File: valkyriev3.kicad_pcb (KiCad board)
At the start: 4 copper layers, 70 x 100 mm, 125 parts, among them J1 USB_C_Receptacle_USB2.0_16P, J10 Conn_01x03, J11 Conn_01x03, J2 DE9_Pins_MountingHoles, J3 SMA_180C, J4 SMA_180C, J5 Conn_01x02_Socket, J6 Conn_01x02_Socket, J7 Conn_01x02_Socket, J8 Conn_01x03, J9 Conn_01x05, Q1 BC817, Q2 BC817, Q3 BC817, Q4 BC817, Q5 BC817, Q6 DMG3420U, Q7 DMP2305U, Q8 DMG3420U, SW1 SW_SPST, SW2 SW_SPST, U1 W25Q128JVS, U10 LPS22HB, U2 ESP32-S3-MINI-1U, U3 MAX3232, U4 AMS1117-3.3, U5 TPS562202, U9 MS5607-02BA

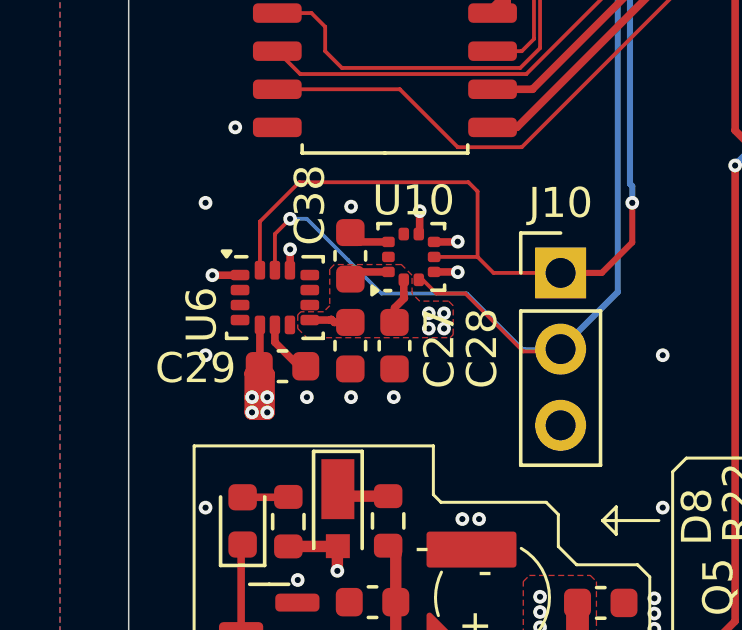
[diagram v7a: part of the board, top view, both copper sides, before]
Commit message: connected IMU pins 7 and 9 to GND instead of NC
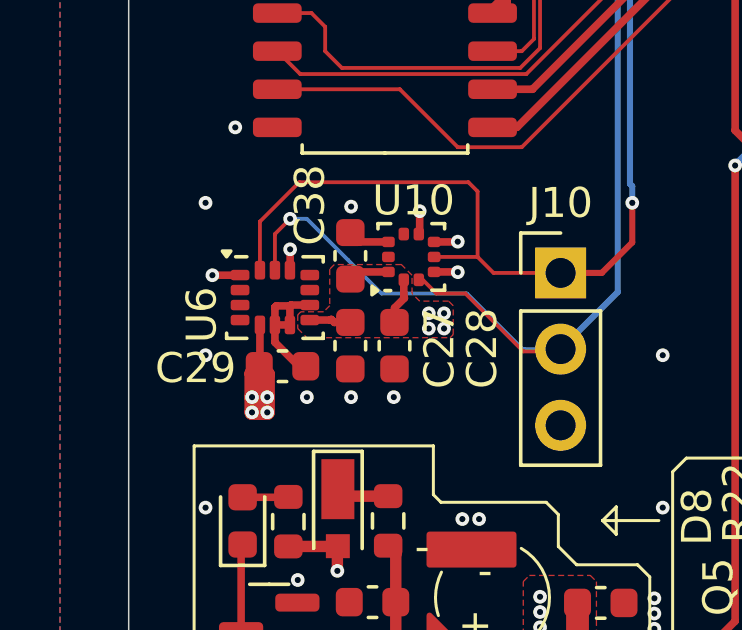
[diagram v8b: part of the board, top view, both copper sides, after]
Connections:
- U6 pad 7: unconnected-(U6-RESV-Pad7) -> GND
- U6 pad 9: unconnected-(U6-INT2/FSYNC-Pad9) -> GND
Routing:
- net GND: track 18.5 -> 21.4 mm
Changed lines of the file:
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@@
 	(net 96 "unconnected-(U6-RESV-Pad10)")
 	(net 97 "unconnected-(U6-RESV-Pad11)")
-	(net 98 "unconnected-(U6-RESV-Pad7)")
-	(net 99 "unconnected-(U6-RESV-Pad3)")
-	(net 100 "unconnected-(U6-RESV-Pad2)")
-	(net 101 "unconnected-(U6-INT1{slash}INT-Pad4)")
-	(net 102 "unconnected-(U6-INT2{slash}FSYNC-Pad9)")
-	(net 103 "unconnected-(U7-FORCE_ON-Pad7)")
-	(net 104 "unconnected-(U7-AADET_N-Pad8)")
-	(net 105 "unconnected-(U7-NC-Pad9)")
-	(net 106 "unconnected-(U8-NC-Pad20)")
-	(net 107 "unconnected-(U8-NC-Pad18)")
-	(net 108 "unconnected-(U8-NC-Pad21)")
-	(net 109 "unconnected-(U8-NC-Pad19)")
-	(net 110 "unconnected-(U8-NC-Pad24)")
-	(net 111 "unconnected-(U9-SDO-Pad6)")
-	(net 112 "unconnected-(U10-INT_DRDY-Pad7)")
-	(net 113 "unconnected-(U2-IO13-Pad17)")
-	(net 114 "unconnected-(U2-IO12-Pad16)")
-	(net 115 "/Connectors/DROGUE_ANODE")
-	(net 116 "ESP_RXD1")
+	(net 98 "unconnected-(U6-RESV-Pad3)")
+	(net 99 "unconnected-(U6-RESV-Pad2)")
+	(net 100 "unconnected-(U6-INT1{slash}INT-Pad4)")
+	(net 101 "unconnected-(U7-FORCE_ON-Pad7)")
+	(net 102 "unconnected-(U7-AADET_N-Pad8)")
+	(net 103 "unconnected-(U7-NC-Pad9)")
+	(net 104 "unconnected-(U8-NC-Pad20)")
+	(net 105 "unconnected-(U8-NC-Pad18)")
+	(net 106 "unconnected-(U8-NC-Pad21)")
+	(net 107 "unconnected-(U8-NC-Pad19)")
+	(net 108 "unconnected-(U8-NC-Pad24)")
+	(net 109 "unconnected-(U9-SDO-Pad6)")
+	(net 110 "unconnected-(U10-INT_DRDY-Pad7)")
+	(net 111 "unconnected-(U2-IO13-Pad17)")
+	(net 112 "unconnected-(U2-IO12-Pad16)")
+	(net 113 "/Connectors/DROGUE_ANODE")
+	(net 114 "ESP_RXD1")
 	(footprint "Package_LGA:LGA-8_3x5mm_P1.25mm"
 		(layer "F.Cu")
@@
 			(size 0.95 0.55)
 			(layers "F.Cu" "F.Mask" "F.Paste")
-			(net 111 "unconnected-(U9-SDO-Pad6)")
+			(net 109 "unconnected-(U9-SDO-Pad6)")
 			(pinfunction "SDO")
 			(pintype "output+no_connect")
@@
 			(layers "F.Cu" "F.Mask" "F.Paste")
 			(roundrect_rratio 0.1086956522)
-			(net 115 "/Connectors/DROGUE_ANODE")
+			(net 113 "/Connectors/DROGUE_ANODE")
 			(pinfunction "A")
 			(pintype "passive")
@@
 			(layers "F.Cu" "F.Mask" "F.Paste")
 			(roundrect_rratio 0.25)
-			(net 100 "unconnected-(U6-RESV-Pad2)")
+			(net 99 "unconnected-(U6-RESV-Pad2)")
 			(pinfunction "RESV")
 			(pintype "passive+no_connect")
@@
 			(layers "F.Cu" "F.Mask" "F.Paste")
 			(roundrect_rratio 0.25)
-			(net 99 "unconnected-(U6-RESV-Pad3)")
+			(net 98 "unconnected-(U6-RESV-Pad3)")
 			(pinfunction "RESV")
 			(pintype "passive+no_connect")
@@
 			(layers "F.Cu" "F.Mask" "F.Paste")
 			(roundrect_rratio 0.25)
-			(net 101 "unconnected-(U6-INT1{slash}INT-Pad4)")
+			(net 100 "unconnected-(U6-INT1{slash}INT-Pad4)")
 			(pinfunction "INT1/INT")
 			(pintype "bidirectional+no_connect")
@@
 			(layers "F.Cu" "F.Mask" "F.Paste")
 			(roundrect_rratio 0.25)
-			(net 98 "unconnected-(U6-RESV-Pad7)")
+			(net 2 "GND")
 			(pinfunction "RESV")
-			(pintype "passive+no_connect")
+			(pintype "passive")
 		)
 		(pad "8" smd roundrect
@@
 			(layers "F.Cu" "F.Mask" "F.Paste")
 			(roundrect_rratio 0.25)
-			(net 102 "unconnected-(U6-INT2{slash}FSYNC-Pad9)")
+			(net 2 "GND")
 			(pinfunction "INT2/FSYNC")
-			(pintype "bidirectional+no_connect")
+			(pintype "bidirectional")
 		)
 		(pad "10" smd roundrect
@@
 			(layers "F.Cu" "F.Mask" "F.Paste")
 			(roundrect_rratio 0.25)
-			(net 112 "unconnected-(U10-INT_DRDY-Pad7)")
+			(net 110 "unconnected-(U10-INT_DRDY-Pad7)")
 			(pinfunction "INT_DRDY")
 			(pintype "output+no_connect")
@@
 			(remove_unused_layers no)
 			(roundrect_rratio 0.22)
-			(net 115 "/Connectors/DROGUE_ANODE")
+			(net 113 "/Connectors/DROGUE_ANODE")
 			(pinfunction "Pin_1")
 			(pintype "passive")
@@
 			(layers "F.Cu" "F.Mask" "F.Paste")
 			(roundrect_rratio 0.25)
-			(net 103 "unconnected-(U7-FORCE_ON-Pad7)")
+			(net 101 "unconnected-(U7-FORCE_ON-Pad7)")
 			(pinfunction "FORCE_ON")
 			(pintype "input+no_connect")
@@
 			(layers "F.Cu" "F.Mask" "F.Paste")
 			(roundrect_rratio 0.25)
-			(net 104 "unconnected-(U7-AADET_N-Pad8)")
+			(net 102 "unconnected-(U7-AADET_N-Pad8)")
 			(pinfunction "AADET_N")
 			(pintype "output+no_connect")
@@
 			(layers "F.Cu" "F.Mask" "F.Paste")
 			(roundrect_rratio 0.25)
-			(net 105 "unconnected-(U7-NC-Pad9)")
+			(net 103 "unconnected-(U7-NC-Pad9)")
 			(pinfunction "NC")
 			(pintype "no_connect")
@@
 			(layers "*.Cu" "*.Mask")
 			(remove_unused_layers no)
-			(net 116 "ESP_RXD1")
+			(net 114 "ESP_RXD1")
 			(pinfunction "Pin_5")
 			(pintype "passive")
@@
 			(layers "F.Cu" "F.Mask" "F.Paste")
 			(roundrect_rratio 0.25)
-			(net 116 "ESP_RXD1")
+			(net 114 "ESP_RXD1")
 			(pinfunction "RXD")
 			(pintype "input")
@@
 			(layers "F.Cu" "F.Mask" "F.Paste")
 			(roundrect_rratio 0.25)
-			(net 107 "unconnected-(U8-NC-Pad18)")
+			(net 105 "unconnected-(U8-NC-Pad18)")
 			(pinfunction "NC")
 			(pintype "no_connect")
@@
 			(layers "F.Cu" "F.Mask" "F.Paste")
 			(roundrect_rratio 0.25)
-			(net 109 "unconnected-(U8-NC-Pad19)")
+			(net 107 "unconnected-(U8-NC-Pad19)")
 			(pinfunction "NC")
 			(pintype "no_connect")
@@
 			(layers "F.Cu" "F.Mask" "F.Paste")
 			(roundrect_rratio 0.25)
-			(net 106 "unconnected-(U8-NC-Pad20)")
+			(net 104 "unconnected-(U8-NC-Pad20)")
 			(pinfunction "NC")
 			(pintype "no_connect")
@@
 			(layers "F.Cu" "F.Mask" "F.Paste")
 			(roundrect_rratio 0.25)
-			(net 108 "unconnected-(U8-NC-Pad21)")
+			(net 106 "unconnected-(U8-NC-Pad21)")
 			(pinfunction "NC")
 			(pintype "no_connect")
@@
 			(layers "F.Cu" "F.Mask" "F.Paste")
 			(roundrect_rratio 0.25)
-			(net 110 "unconnected-(U8-NC-Pad24)")
+			(net 108 "unconnected-(U8-NC-Pad24)")
 			(pinfunction "NC")
 			(pintype "no_connect")
@@
 			(size 0.8 0.4)
 			(layers "F.Cu" "F.Mask" "F.Paste")
-			(net 114 "unconnected-(U2-IO12-Pad16)")
+			(net 112 "unconnected-(U2-IO12-Pad16)")
 			(pinfunction "IO12")
 			(pintype "bidirectional+no_connect")
@@
 			(size 0.8 0.4)
 			(layers "F.Cu" "F.Mask" "F.Paste")
-			(net 113 "unconnected-(U2-IO13-Pad17)")
+			(net 111 "unconnected-(U2-IO13-Pad17)")
 			(pinfunction "IO13")
 			(pintype "bidirectional+no_connect")
@@
 			(size 0.8 0.4)
 			(layers "F.Cu" "F.Mask" "F.Paste")
-			(net 116 "ESP_RXD1")
+			(net 114 "ESP_RXD1")
 			(pinfunction "IO18")
 			(pintype "bidirectional")
@@
 	)
 	(segment
+		(start 103.0155 113.2909)
+		(end 103.0434 113.263)
+		(width 0.254)
+		(layer "F.Cu")
+		(net 2)
+	)
+	(segment
 		(start 105.3406 111.1584)
 		(end 105.0294 110.8472)
@@
 	)
 	(segment
+		(start 103.0155 113.9255)
+		(end 103.0155 113.2909)
+		(width 0.254)
+		(layer "F.Cu")
+		(net 2)
+	)
+	(segment
 		(start 105.689 92.1262)
 		(end 105.8672 91.948)
@@
 	)
 	(segment
+		(start 103.0434 113.263)
+		(end 103.678 113.263)
+		(width 0.254)
+		(layer "F.Cu")
+		(net 2)
+	)
+	(segment
 		(start 140.97 123.7966)
 		(end 140.9899 123.7767)
@@
 	)
 	(segment
+		(start 102.5144 113.3348)
+		(end 102.5155 113.3359)
+		(width 0.254)
+		(layer "F.Cu")
+		(net 2)
+	)
+	(segment
 		(start 142.494 124.714)
 		(end 142.494 123.7822)
@@
 	)
 	(segment
+		(start 102.5583 113.2909)
+		(end 102.5144 113.3348)
+		(width 0.254)
+		(layer "F.Cu")
+		(net 2)
+	)
+	(segment
+		(start 102.5155 113.3359)
+		(end 102.5155 113.9255)
+		(width 0.254)
+		(layer "F.Cu")
+		(net 2)
+	)
+	(segment
+		(start 102.5155 113.9255)
+		(end 103.0155 113.9255)
+		(width 0.254)
+		(layer "F.Cu")
+		(net 2)
+	)
+	(segment
 		(start 108.6024 112.1584)
 		(end 108.6104 112.1664)
@@
 	)
 	(segment
+		(start 103.0155 113.2909)
+		(end 102.5583 113.2909)
+		(width 0.254)
+		(layer "F.Cu")
+		(net 2)
+	)
+	(segment
 		(start 149.5044 131.0132)
 		(end 149.5044 130.0186)
@@
 		(width 0.127)
 		(layer "F.Cu")
-		(net 116)
+		(net 114)
 	)
 	(segment
@@
 		(width 0.127)
 		(layer "F.Cu")
-		(net 116)
+		(net 114)
 	)
 	(segment
@@
 		(width 0.127)
 		(layer "F.Cu")
-		(net 116)
+		(net 114)
 	)
 	(segment
@@
 		(width 0.127)
 		(layer "F.Cu")
-		(net 116)
+		(net 114)
 	)
 	(segment
@@
 		(width 0.127)
 		(layer "F.Cu")
-		(net 116)
+		(net 114)
 	)
 	(segment
@@
 		(width 0.127)
 		(layer "F.Cu")
-		(net 116)
+		(net 114)
 	)
 	(segment
@@
 		(width 0.127)
 		(layer "F.Cu")
-		(net 116)
+		(net 114)
 	)
 	(segment
@@
 		(width 0.127)
 		(layer "F.Cu")
-		(net 116)
+		(net 114)
 	)
 	(segment
@@
 		(width 0.127)
 		(layer "F.Cu")
-		(net 116)
+		(net 114)
 	)
 	(segment
@@
 		(width 0.127)
 		(layer "F.Cu")
-		(net 116)
+		(net 114)
 	)
 	(segment
@@
 		(width 0.127)
 		(layer "F.Cu")
-		(net 116)
+		(net 114)
 	)
 	(segment
@@
 		(width 0.127)
 		(layer "F.Cu")
-		(net 116)
+		(net 114)
 	)
 	(zone
-		(net 115)
+		(net 113)
 		(net_name "/Connectors/DROGUE_ANODE")
 		(layer "F.Cu")
